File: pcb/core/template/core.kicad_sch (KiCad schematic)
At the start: 5 parts, among them J1 Conn_01x11, J2 Conn_01x11, U1 Helios

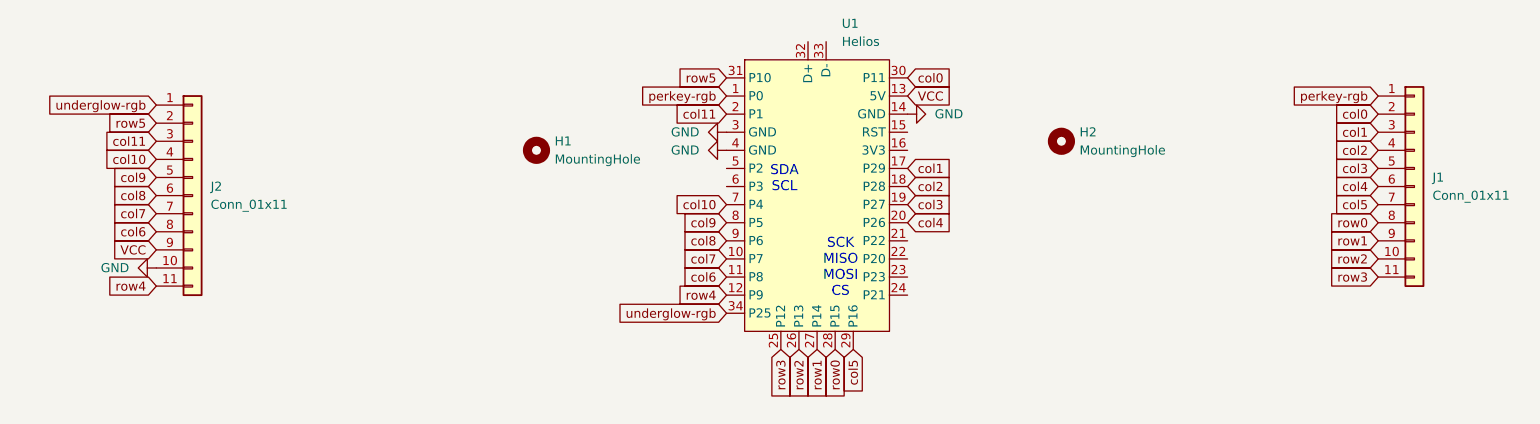
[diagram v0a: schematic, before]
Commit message: added 3x3 core
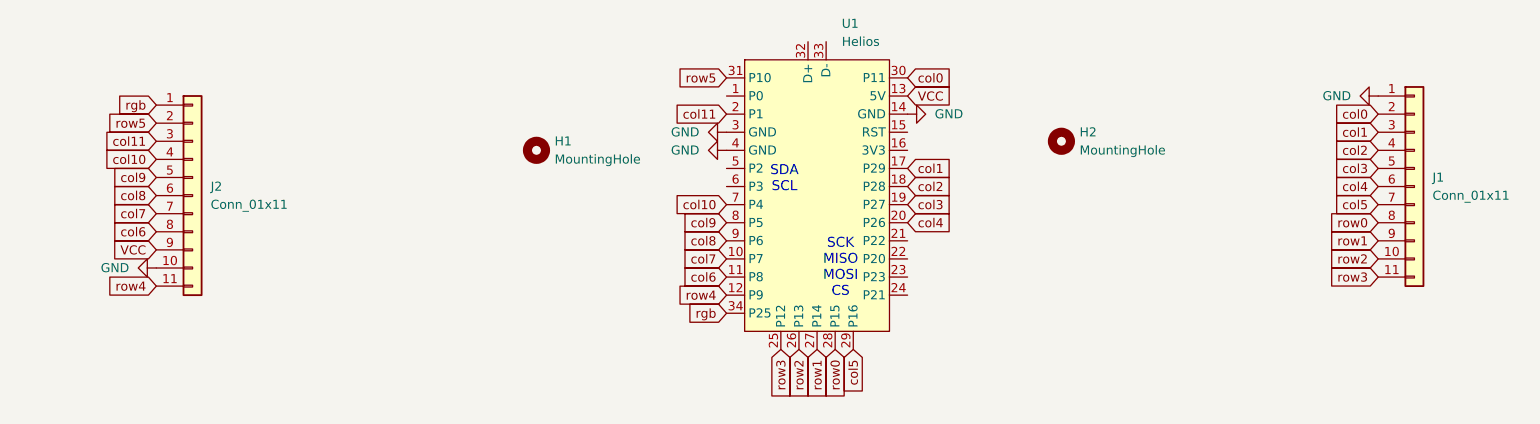
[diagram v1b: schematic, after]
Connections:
- net GND: now also J1.1 (Pin_1)
- net perkey-rgb: no longer names the net of U1.1 (P0)
- net perkey-rgb: no longer J1.1 (Pin_1)
- net underglow-rgb renamed rgb
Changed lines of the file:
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@@
-		)
-	)
-	(global_label "perkey-rgb"
-		(shape input)
-		(at 217.17 53.34 180)
-		(fields_autoplaced yes)
-		(effects
-			(font
-				(size 1.27 1.27)
-			)
-			(justify right)
-		)
-		(property "Intersheetrefs" "${INTERSHEET_REFS}"
-			(at 203.4201 53.34 0)
-			(effects
-				(font
-					(size 1.27 1.27)
-				)
-				(justify right)
-				(hide yes)
-			)
 		)
 	)
@@
 		)
 	)
-	(global_label "underglow-rgb"
+	(global_label "rgb"
 		(shape input)
 		(at 125.73 83.82 180)
@@
 		)
 		(property "Intersheetrefs" "${INTERSHEET_REFS}"
-			(at 108.4727 83.82 0)
+			(at 119.6606 83.82 0)
 			(effects
 				(font
@@
 		)
 	)
-	(global_label "underglow-rgb"
+	(global_label "rgb"
 		(shape input)
 		(at 45.72 54.61 180)
@@
 		)
 		(property "Intersheetrefs" "${INTERSHEET_REFS}"
-			(at 28.4627 54.61 0)
+			(at 39.6506 54.61 0)
 			(effects
 				(font
@@
 		(property "Intersheetrefs" "${INTERSHEET_REFS}"
 			(at 210.0725 66.04 0)
-			(effects
-				(font
-					(size 1.27 1.27)
-				)
-				(justify right)
-				(hide yes)
-			)
-		)
-	)
-	(global_label "perkey-rgb"
-		(shape input)
-		(at 125.73 53.34 180)
-		(fields_autoplaced yes)
-		(effects
-			(font
-				(size 1.27 1.27)
-			)
-			(justify right)
-		)
-		(property "Intersheetrefs" "${INTERSHEET_REFS}"
-			(at 111.9801 53.34 0)
 			(effects
 				(font
@@
 					(unit 1)
 				)
+			)
+		)
+	)
+	(symbol
+		(lib_id "power:GND")
+		(at 217.17 53.34 270)
+		(unit 1)
+		(exclude_from_sim no)
+		(in_bom yes)
+		(on_board yes)
+		(dnp no)
+		(fields_autoplaced yes)
+		(property "Reference" "#PWR05"
+			(at 210.82 53.34 0)
+			(effects
+				(font
+					(size 1.27 1.27)
+				)
+				(hide yes)
+			)
+		)
+		(property "Value" "GND"
+			(at 213.36 53.3399 90)
+			(effects
+				(font
+					(size 1.27 1.27)
+				)
+				(justify right)
+			)
+		)
+		(property "Footprint" ""
+			(at 217.17 53.34 0)
+			(effects
+				(font
+					(size 1.27 1.27)
+				)
+				(hide yes)
+			)
+		)
+		(property "Datasheet" ""
+			(at 217.17 53.34 0)
+			(effects
+				(font
+					(size 1.27 1.27)
+				)
+				(hide yes)
+			)
+		)
+		(property "Description" "Power symbol creates a global label with name \"GND\" , ground"
+			(at 217.17 53.34 0)
+			(effects
+				(font
+					(size 1.27 1.27)
+				)
+				(hide yes)
+			)
+		)
+		(pin "1"
+		)
+		(instances
+			(project "core"
+				(path "/8ef1751a-3bdc-4956-a5e1-70d94fb666d4"
+					(reference "#PWR05")
+					(unit 1)
+				)

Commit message: switched rgb back to a regular pin and 3v
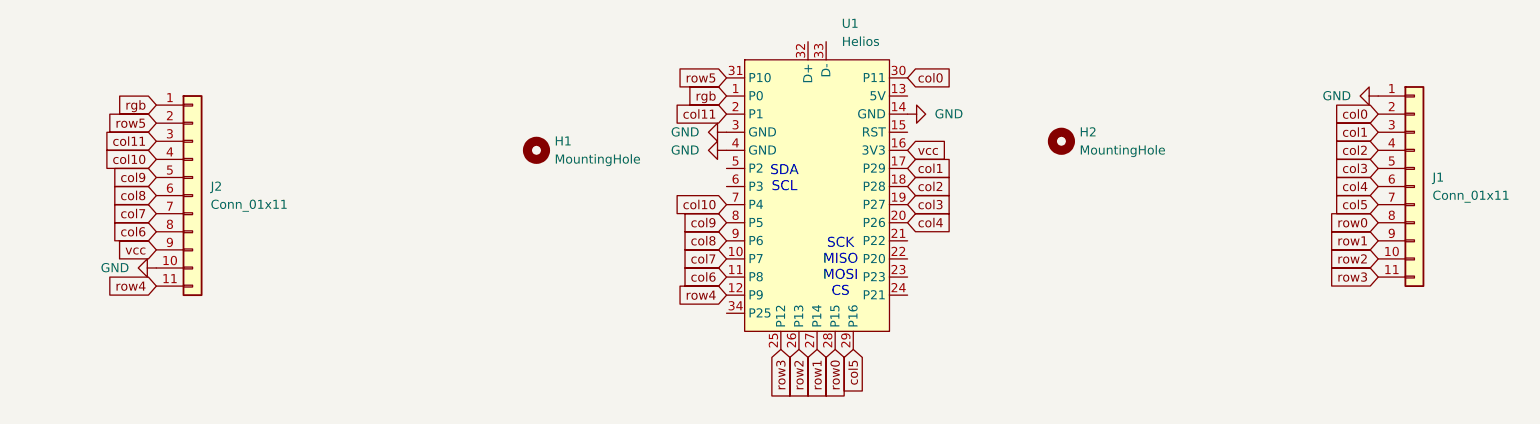
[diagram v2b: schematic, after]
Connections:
- net rgb: now also U1.1 (P0); no longer U1.34 (P25)
- net vcc: now reaches U1.16 (3V3)
- net vcc: now also J2.9 (Pin_9)
- net VCC: no longer names the net of U1.13 (5V)
- net VCC: no longer J2.9 (Pin_9)
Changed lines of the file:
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@@
+		)
+	)
+	(global_label "vcc"
+		(shape input)
+		(at 151.13 60.96 0)
+		(fields_autoplaced yes)
+		(effects
+			(font
+				(size 1.27 1.27)
+			)
+			(justify left)
+		)
+		(property "Intersheetrefs" "${INTERSHEET_REFS}"
+			(at 157.26 60.96 0)
+			(effects
+				(font
+					(size 1.27 1.27)
+				)
+				(justify left)
+				(hide yes)
+			)
 		)
 	)
@@
 	(global_label "rgb"
 		(shape input)
-		(at 125.73 83.82 180)
-		(fields_autoplaced yes)
-		(effects
-			(font
-				(size 1.27 1.27)
-			)
-			(justify right)
-		)
-		(property "Intersheetrefs" "${INTERSHEET_REFS}"
-			(at 119.6606 83.82 0)
+		(at 125.73 53.34 180)
+		(fields_autoplaced yes)
+		(effects
+			(font
+				(size 1.27 1.27)
+			)
+			(justify right)
+		)
+		(property "Intersheetrefs" "${INTERSHEET_REFS}"
+			(at 119.6606 53.34 0)
 			(effects
 				(font
@@
 		)
 	)
-	(global_label "VCC"
+	(global_label "vcc"
 		(shape input)
 		(at 45.72 74.93 180)
@@
 		)
 		(property "Intersheetrefs" "${INTERSHEET_REFS}"
-			(at 39.1062 74.93 0)
+			(at 39.59 74.93 0)
 			(effects
 				(font
@@
 				(hide yes)
 			)
-		)
-	)
-	(global_label "VCC"
-		(shape input)
-		(at 151.13 53.34 0)
-		(fields_autoplaced yes)
-		(effects
-			(font
-				(size 1.27 1.27)
-			)
-			(justify left)
-		)
-		(property "Intersheetrefs" "${INTERSHEET_REFS}"
-			(at 157.7438 53.34 0)
-			(effects
-				(font
-					(size 1.27 1.27)
-				)
-				(justify left)
-				(hide yes)
-			)

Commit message: added jumpers for 3.3/5v rgb
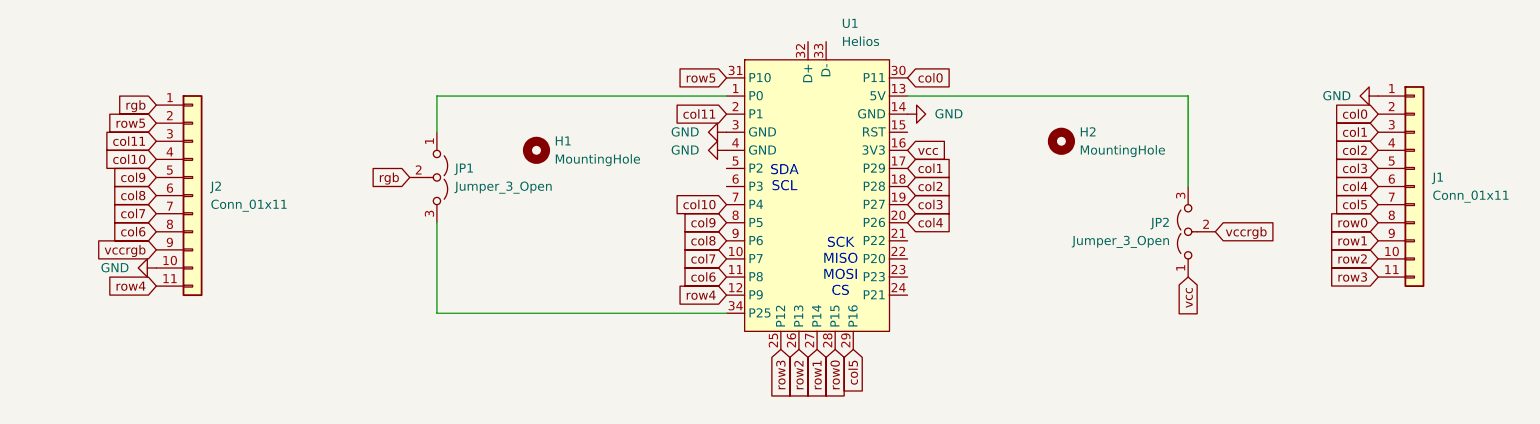
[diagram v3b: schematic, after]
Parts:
- added JP1, JP2: Jumper_3_Open, Jumper:SolderJumper-3_P1.3mm_Open_RoundedPad1.0x1.5mm, symbol Jumper:Jumper_3_Open
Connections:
- net rgb: now also JP1.2 (C); no longer U1.1 (P0)
- net vcc: now also JP2.1 (A); no longer J2.9 (Pin_9)
- net at U1.13 (5V): now also JP2.3 (B)
- net at U1.34 (P25): now also JP1.3 (B)
- new net: JP1.1 (A), U1.1 (P0)
- new net vccrgb: J2.9 (Pin_9), JP2.2 (C)
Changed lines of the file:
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@@
 	(generator_version "8.0")
 	(paper "A4")
+	(wire
+		(pts
+			(xy 85.09 53.34) (xy 85.09 58.42)
+		)
+		(stroke
+			(width 0)
+			(type default)
+		)
+	)
+	(wire
+		(pts
+			(xy 125.73 53.34) (xy 85.09 53.34)
+		)
+		(stroke
+			(width 0)
+			(type default)
+		)
+	)
+	(wire
+		(pts
+			(xy 151.13 53.34) (xy 190.5 53.34)
+		)
+		(stroke
+			(width 0)
+			(type default)
+		)
+	)
+	(wire
+		(pts
+			(xy 85.09 71.12) (xy 85.09 83.82)
+		)
+		(stroke
+			(width 0)
+			(type default)
+		)
+	)
+	(wire
+		(pts
+			(xy 190.5 53.34) (xy 190.5 66.04)
+		)
+		(stroke
+			(width 0)
+			(type default)
+		)
+	)
+	(wire
+		(pts
+			(xy 85.09 83.82) (xy 125.73 83.82)
+		)
+		(stroke
+			(width 0)
+			(type default)
+		)
+	)
 	(text "SDA\nSCL"
 		(exclude_from_sim no)
@@
 		)
 	)
+	(global_label "vcc"
+		(shape input)
+		(at 190.5 78.74 270)
+		(fields_autoplaced yes)
+		(effects
+			(font
+				(size 1.27 1.27)
+			)
+			(justify right)
+		)
+		(property "Intersheetrefs" "${INTERSHEET_REFS}"
+			(at 190.5 84.87 90)
+			(effects
+				(font
+					(size 1.27 1.27)
+				)
+				(justify right)
+				(hide yes)
+			)
+		)
+	)
 	(global_label "col2"
 		(shape input)
@@
 		)
 	)
+	(global_label "vccrgb"
+		(shape input)
+		(at 194.31 72.39 0)
+		(fields_autoplaced yes)
+		(effects
+			(font
+				(size 1.27 1.27)
+			)
+			(justify left)
+		)
+		(property "Intersheetrefs" "${INTERSHEET_REFS}"
+			(at 203.5242 72.39 0)
+			(effects
+				(font
+					(size 1.27 1.27)
+				)
+				(justify left)
+				(hide yes)
+			)
+		)
+	)
 	(global_label "col10"
 		(shape input)
@@
 		)
 	)
+	(global_label "col9"
+		(shape input)
+		(at 45.72 64.77 180)
+		(fields_autoplaced yes)
+		(effects
+			(font
+				(size 1.27 1.27)
+			)
+			(justify right)
+		)
+		(property "Intersheetrefs" "${INTERSHEET_REFS}"
+			(at 38.6225 64.77 0)
+			(effects
+				(font
+					(size 1.27 1.27)
+				)
+				(justify right)
+				(hide yes)
+			)
+		)
+	)
+	(global_label "col11"
+		(shape input)
+		(at 45.72 59.69 180)
+		(fields_autoplaced yes)
+		(effects
+			(font
+				(size 1.27 1.27)
+			)
+			(justify right)
+		)
+		(property "Intersheetrefs" "${INTERSHEET_REFS}"
+			(at 37.413 59.69 0)
+			(effects
+				(font
+					(size 1.27 1.27)
+				)
+				(justify right)
+				(hide yes)
+			)
+		)
+	)
 	(global_label "rgb"
 		(shape input)
-		(at 125.73 53.34 180)
-		(fields_autoplaced yes)
-		(effects
-			(font
-				(size 1.27 1.27)
-			)
-			(justify right)
-		)
-		(property "Intersheetrefs" "${INTERSHEET_REFS}"
-			(at 119.6606 53.34 0)
-			(effects
-				(font
-					(size 1.27 1.27)
-				)
-				(justify right)
-				(hide yes)
-			)
-		)
-	)
-	(global_label "col9"
-		(shape input)
-		(at 45.72 64.77 180)
-		(fields_autoplaced yes)
-		(effects
-			(font
-				(size 1.27 1.27)
-			)
-			(justify right)
-		)
-		(property "Intersheetrefs" "${INTERSHEET_REFS}"
-			(at 38.6225 64.77 0)
-			(effects
-				(font
-					(size 1.27 1.27)
-				)
-				(justify right)
-				(hide yes)
-			)
-		)
-	)
-	(global_label "col11"
-		(shape input)
-		(at 45.72 59.69 180)
-		(fields_autoplaced yes)
-		(effects
-			(font
-				(size 1.27 1.27)
-			)
-			(justify right)
-		)
-		(property "Intersheetrefs" "${INTERSHEET_REFS}"
-			(at 37.413 59.69 0)
+		(at 45.72 54.61 180)
+		(fields_autoplaced yes)
+		(effects
+			(font
+				(size 1.27 1.27)
+			)
+			(justify right)
+		)
+		(property "Intersheetrefs" "${INTERSHEET_REFS}"
+			(at 39.6506 54.61 0)
+			(effects
+				(font
+					(size 1.27 1.27)
+				)
+				(justify right)
+				(hide yes)
+			)
+		)
+	)
+	(global_label "vccrgb"
+		(shape input)
+		(at 45.72 74.93 180)
+		(fields_autoplaced yes)
+		(effects
+			(font
+				(size 1.27 1.27)
+			)
+			(justify right)
+		)
+		(property "Intersheetrefs" "${INTERSHEET_REFS}"
+			(at 36.5058 74.93 0)
 			(effects
 				(font
@@
 	(global_label "rgb"
 		(shape input)
-		(at 45.72 54.61 180)
-		(fields_autoplaced yes)
-		(effects
-			(font
-				(size 1.27 1.27)
-			)
-			(justify right)
-		)
-		(property "Intersheetrefs" "${INTERSHEET_REFS}"
-			(at 39.6506 54.61 0)
-			(effects
-				(font
-					(size 1.27 1.27)
-				)
-				(justify right)
-				(hide yes)
-			)
-		)
-	)
-	(global_label "vcc"
-		(shape input)
-		(at 45.72 74.93 180)
-		(fields_autoplaced yes)
-		(effects
-			(font
-				(size 1.27 1.27)
-			)
-			(justify right)
-		)
-		(property "Intersheetrefs" "${INTERSHEET_REFS}"
-			(at 39.59 74.93 0)
+		(at 81.28 64.77 180)
+		(fields_autoplaced yes)
+		(effects
+			(font
+				(size 1.27 1.27)
+			)
+			(justify right)
+		)
+		(property "Intersheetrefs" "${INTERSHEET_REFS}"
+			(at 75.2106 64.77 0)
 			(effects
 				(font
@@
 	)
 	(symbol
+		(lib_id "Jumper:Jumper_3_Open")
+		(at 85.09 64.77 270)
+		(unit 1)
+		(exclude_from_sim yes)
+		(in_bom no)
+		(on_board yes)
+		(dnp no)
+		(fields_autoplaced yes)
+		(property "Reference" "JP1"
+			(at 87.63 63.4999 90)
+			(effects
+				(font
+					(size 1.27 1.27)
+				)
+				(justify left)
+			)
+		)
+		(property "Value" "Jumper_3_Open"
+			(at 87.63 66.0399 90)
+			(effects
+				(font
+					(size 1.27 1.27)
+				)
+				(justify left)
+			)
+		)
+		(property "Footprint" "Jumper:SolderJumper-3_P1.3mm_Open_RoundedPad1.0x1.5mm"
+			(at 85.09 64.77 0)
+			(effects
+				(font
+					(size 1.27 1.27)
+				)
+				(hide yes)
+			)
+		)
+		(property "Datasheet" "~"
+			(at 85.09 64.77 0)
+			(effects
+				(font
+					(size 1.27 1.27)
+				)
+				(hide yes)
+			)
+		)
+		(property "Description" "Jumper, 3-pole, both open"
+			(at 85.09 64.77 0)
+			(effects
+				(font
+					(size 1.27 1.27)
+				)
+				(hide yes)
+			)
+		)
+		(pin "3"
+		)
+		(pin "2"
+		)
+		(pin "1"
+		)
+		(instances
+			(project ""
+				(path "/8ef1751a-3bdc-4956-a5e1-70d94fb666d4"
+					(reference "JP1")
+					(unit 1)
+				)
+			)
+		)
+	)
+	(symbol
 		(lib_id "power:GND")
 		(at 125.73 60.96 270)
@@
 					(unit 1)
 				)
+			)
+		)
+	)
+	(symbol
+		(lib_id "Jumper:Jumper_3_Open")
+		(at 190.5 72.39 90)
+		(unit 1)
+		(exclude_from_sim yes)
+		(in_bom no)
+		(on_board yes)
+		(dnp no)
+		(fields_autoplaced yes)
+		(property "Reference" "JP2"
+			(at 187.96 71.1199 90)
+			(effects
+				(font
+					(size 1.27 1.27)
+				)
+				(justify left)
+			)
+		)
+		(property "Value" "Jumper_3_Open"
+			(at 187.96 73.6599 90)
+			(effects
+				(font
+					(size 1.27 1.27)
+				)
+				(justify left)
+			)
+		)
+		(property "Footprint" "Jumper:SolderJumper-3_P1.3mm_Open_RoundedPad1.0x1.5mm"
+			(at 190.5 72.39 0)
+			(effects
+				(font
+					(size 1.27 1.27)
+				)
+				(hide yes)
+			)
+		)
+		(property "Datasheet" "~"
+			(at 190.5 72.39 0)
+			(effects
+				(font
+					(size 1.27 1.27)
+				)
+				(hide yes)
+			)
+		)
+		(property "Description" "Jumper, 3-pole, both open"
+			(at 190.5 72.39 0)
+			(effects
+				(font
+					(size 1.27 1.27)
+				)
+				(hide yes)
+			)
+		)
+		(pin "3"
+		)
+		(pin "2"
+		)
+		(pin "1"
+		)
+		(instances
+			(project "core"
+				(path "/8ef1751a-3bdc-4956-a5e1-70d94fb666d4"
+					(reference "JP2")
+					(unit 1)
+				)
